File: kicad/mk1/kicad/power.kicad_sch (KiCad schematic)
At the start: 32 parts, among them J1 Barrel_Jack, U2 AP64501SP-13, U9 BSZ040N04LSGATMA1

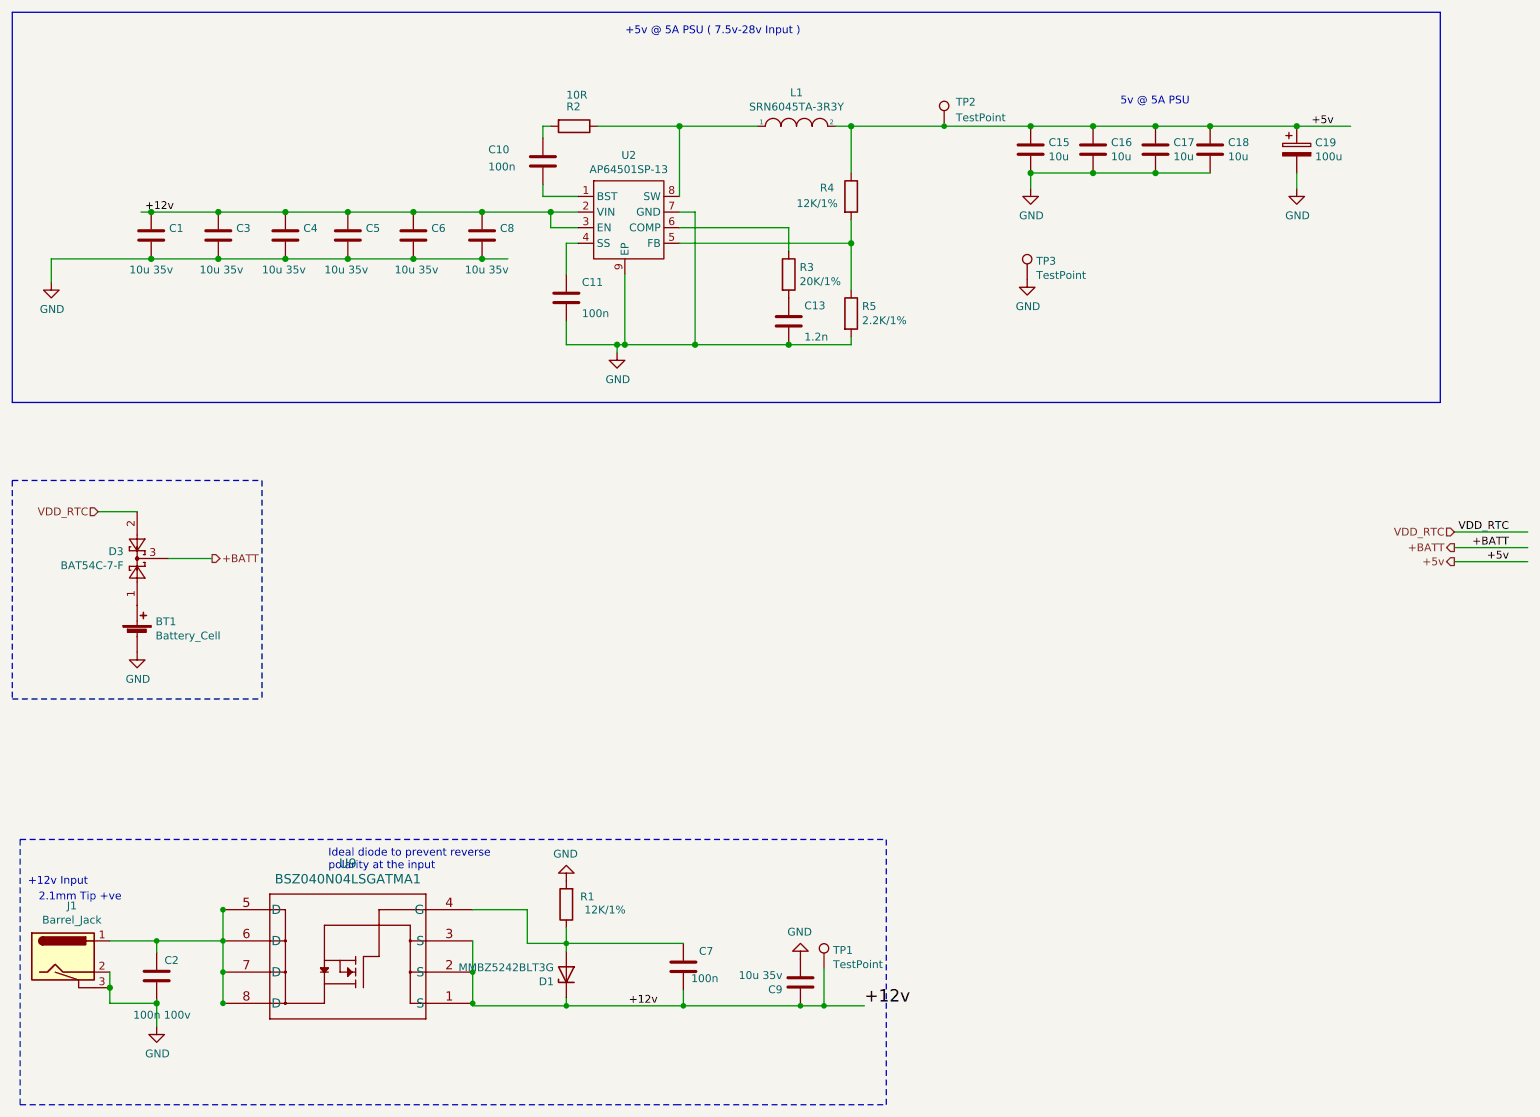
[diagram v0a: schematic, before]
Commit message: work on schematics
* add power rail
* import CM4 related part
* design most of the BMC-PHY part
* create new library/footprint for rp t113-s3 SOM
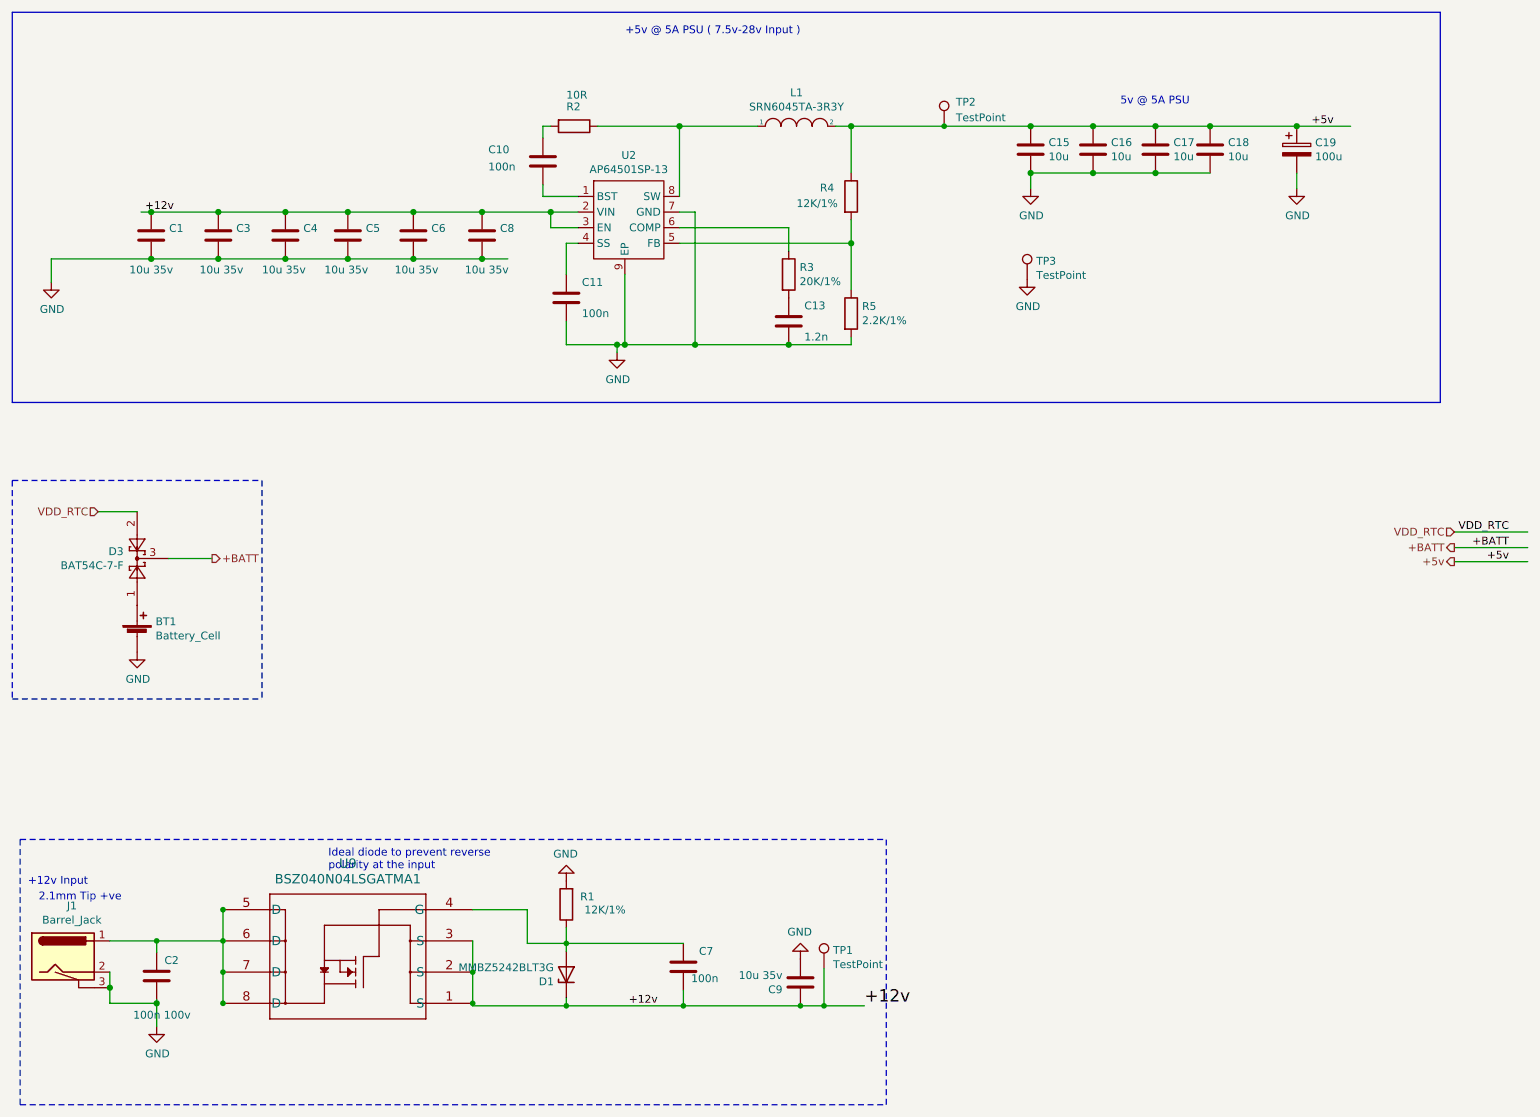
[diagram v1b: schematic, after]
